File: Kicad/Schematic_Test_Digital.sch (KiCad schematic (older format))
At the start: 73 parts, among them J301 JST - 4x1, J302 JST - 4x1, J303 JST - 5x1, J304 JST - 5x1, SW301 RESET PUSH, U301 TSX-3225, U302 LIS3MDLTR, U303 LSM6DS33TR, U304 74HC595PW,112, U305 74HC595PW,112, U306 74HC595PW,112

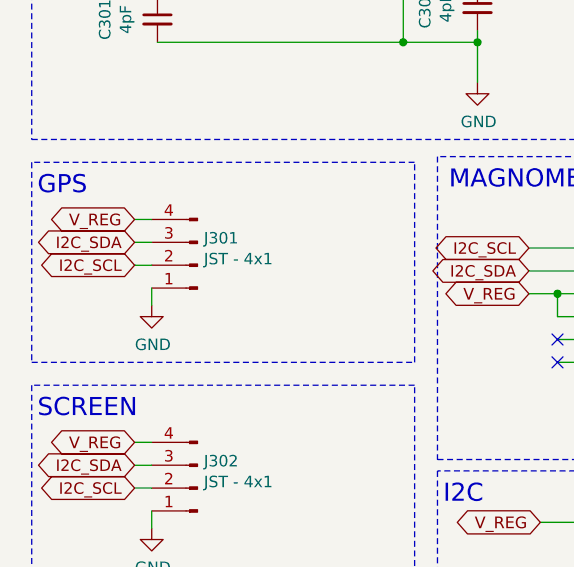
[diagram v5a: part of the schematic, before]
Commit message: PCB is likely complete.  Added USART for GPS.  Added background art and front label. Some leftover things are needed for the case.
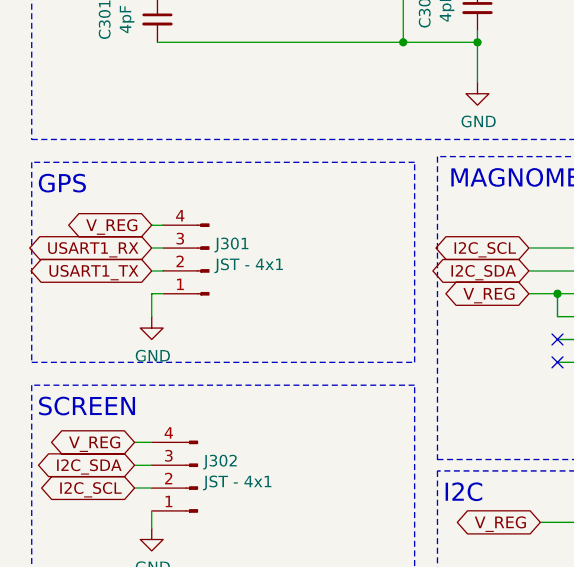
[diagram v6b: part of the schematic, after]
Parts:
- J301: part_details (none) -> USART; part_url (none) -> https://www.amazon.com/Microcontroller-Compatible-Sensitivi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
- J302: part_details (none) -> I2C; part_url https://www.amazon.com/WayinTop-Display-SSD1306-3-3V-5V-Ras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 -> https://www.amazon.com/Pieces-Display-Module-SSD1306-3-3V-5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
- J304: part_details (none) -> I2C; part_url (none) -> https://www.amazon.com/ARCELI-Joystick-Controller-Dual-axis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
- R302, R303: part_name Resistor - Pull up -> Resistor - Pull Up
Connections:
- net I2C_SCL: no longer J301.2 (Pin_2)
- net I2C_SDA: no longer J301.3 (Pin_3)
- new net USART1_RX: J301.3 (Pin_3)
- new net USART1_TX: J301.2 (Pin_2)
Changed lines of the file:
@@
 F 2 "Connector_JST:JST_EH_B5B-EH-A_1x05_P2.50mm_Vertical" H 1650 6025 50  0001 C CNN
 F 3 "~" H 1650 6025 50  0001 C CNN
-F 4 "" H 1650 6025 50  0001 C CNN "part_details"
-F 5 "" H 1650 6025 50  0001 C CNN "part_url"
+F 4 "I2C" H 1650 6025 50  0001 C CNN "part_details"
+F 5 "https://www.amazon.com/ARCELI-Joystick-Controller-Dual-axis-Breakout/dp/B077Z8QN3S" H 1650 6025 50  0001 C CNN "part_url"
 F 6 "Joystick Connector" H 1650 6025 50  0001 C CNN "part_name"
 	1    1650 6025
@@
 F 2 "Connector_JST:JST_EH_B4B-EH-A_1x04_P2.50mm_Vertical" H 1300 5050 50  0001 C CNN
 F 3 "~" H 1300 5050 50  0001 C CNN
-F 4 "" H 1300 5050 50  0001 C CNN "part_details"
-F 5 "https://www.amazon.com/WayinTop-Display-SSD1306-3-3V-5V-Raspberry/dp/B085NHJYBV/ref=pd_vtp_328_10?_encoding=UTF8&pd_rd_i=B085NHM5TC&pd_rd_r=7bdf7370-03dc-4b29-82c0-f607778b8952&pd_rd_w=HTH0F&pd_rd_wg=QAfMe&pf_rd_p=9f0d957d-c466-420a-817f-4adcb2657c85&pf_rd_r=2740EXSJPY7P7H0NYG2V&refRID=2740EXSJPY7P7H0NYG2V&th=1" H 1300 5050 50  0001 C CNN "part_url"
+F 4 "I2C" H 1300 5050 50  0001 C CNN "part_details"
+F 5 "https://www.amazon.com/Pieces-Display-Module-SSD1306-3-3V-5V/dp/B08CDN5PSJ/ref=pd_sbs_147_4/145-1111266-3690268?_encoding=UTF8&pd_rd_i=B08CDN5PSJ&pd_rd_r=0e37c7d0-00d4-4c6c-b496-f9da0ffda669&pd_rd_w=mtWFO&pd_rd_wg=RCtoO&pf_rd_p=703f3758-d945-4136-8df6-a43d19d750d1&pf_rd_r=FBPTKKC3JN25YH77MA03&psc=1&refRID=FBPTKKC3JN25YH77MA03" H 1300 5050 50  0001 C CNN "part_url"
 F 6 "Screen Connector" H 1300 5050 50  0001 C CNN "part_name"
 	1    1300 5050
@@
 Wire Notes Line
 	575  4500 2250 4500
-Wire Wire Line
-	1025 3875 1100 3875
-Wire Wire Line
-	1025 4075 1100 4075
-Wire Wire Line
-	1025 3975 1100 3975
 Wire Notes Line
 	2250 3625 575  3625
@@
 Wire Notes Line
 	575  3625 575  4500
-$Comp
-L power:GND #PWR?
-U 1 1 5F64B2EE
-P 1100 4250
-AR Path="/5F64B2EE" Ref="#PWR?"  Part="1"
-AR Path="/5F580392/5F64B2EE" Ref="#PWR0302"  Part="1"
-F 0 "#PWR0302" H 1100 4000 50  0001 C CNN
-F 1 "GND" H 1105 4077 50  0000 C CNN
-F 2 "" H 1100 4250 50  0001 C CNN
-F 3 "" H 1100 4250 50  0001 C CNN
-	1    1100 4250
-	1    0    0    -1
-$EndComp
-Wire Wire Line
-	1100 4175 1100 4250
-$Comp
-L Connector:Conn_01x04_Male J?
-U 1 1 5F64B2F5
-P 1300 4075
-AR Path="/5F64B2F5" Ref="J?"  Part="1"
-AR Path="/5F580392/5F64B2F5" Ref="J301"  Part="1"
-F 0 "J301" H 1272 3957 50  0000 R CNN
-F 1 "JST - 4x1" H 1272 4048 50  0000 R CNN
-F 2 "Connector_JST:JST_EH_B4B-EH-A_1x04_P2.50mm_Vertical" H 1300 4075 50  0001 C CNN
-F 3 "~" H 1300 4075 50  0001 C CNN
-F 4 "" H 1300 4075 50  0001 C CNN "part_details"
-F 5 "" H 1300 4075 50  0001 C CNN "part_url"
-F 6 "GPS Connector" H 1300 4075 50  0001 C CNN "part_name"
-	1    1300 4075
-	-1   0    0    1
-$EndComp
-Text Notes 600  3775 0    79   ~ 0
-GPS\n
-Text GLabel 1025 3975 0    50   BiDi ~ 0
-I2C_SDA
-Text GLabel 1025 4075 0    50   BiDi ~ 0
-I2C_SCL
-Text GLabel 1025 3875 0    51   BiDi ~ 0
-V_REG
 Connection ~ 10700 4900
 Wire Wire Line
@@
 F 2 "Resistor_SMD:R_1206_3216Metric_Pad1.42x1.75mm_HandSolder" V 3430 5525 50  0001 C CNN
 F 3 "~" H 3500 5525 50  0001 C CNN
-F 4 "Resistor - Pull up" H 3500 5525 50  0001 C CNN "part_name"
+F 4 "Resistor - Pull Up" H 3500 5525 50  0001 C CNN "part_name"
 F 5 "https://www.digikey.com/product-detail/en/yageo/RC1206JR-0710KL/311-10KERCT-ND/732156" H 3500 5525 50  0001 C CNN "part_url"
 	1    3500 5525
@@
 F 2 "Resistor_SMD:R_1206_3216Metric_Pad1.42x1.75mm_HandSolder" V 3080 5525 50  0001 C CNN
 F 3 "~" H 3150 5525 50  0001 C CNN
-F 4 "Resistor - Pull up" H 3150 5525 50  0001 C CNN "part_name"
+F 4 "Resistor - Pull Up" H 3150 5525 50  0001 C CNN "part_name"
 F 5 "https://www.digikey.com/product-detail/en/yageo/RC1206JR-0710KL/311-10KERCT-ND/732156" H 3150 5525 50  0001 C CNN "part_url"
 	1    3150 5525
@@
 Text GLabel 8300 3425 0    50   BiDi ~ 0
 RESET_N
+$Comp
+L power:GND #PWR?
+U 1 1 5F94CCE4
+P 1100 4300
+AR Path="/5F94CCE4" Ref="#PWR?"  Part="1"
+AR Path="/5F580392/5F94CCE4" Ref="#PWR0107"  Part="1"
+F 0 "#PWR0107" H 1100 4050 50  0001 C CNN
+F 1 "GND" H 1105 4127 50  0000 C CNN
+F 2 "" H 1100 4300 50  0001 C CNN
+F 3 "" H 1100 4300 50  0001 C CNN
+	1    1100 4300
+	1    0    0    -1
+$EndComp
+$Comp
+L Connector:Conn_01x04_Male J?
+U 1 1 5F94CCED
+P 1350 4100
+AR Path="/5F94CCED" Ref="J?"  Part="1"
+AR Path="/5F580392/5F94CCED" Ref="J301"  Part="1"
+F 0 "J301" H 1322 3982 50  0000 R CNN
+F 1 "JST - 4x1" H 1322 4073 50  0000 R CNN
+F 2 "Connector_JST:JST_EH_B4B-EH-A_1x04_P2.50mm_Vertical" H 1350 4100 50  0001 C CNN
+F 3 "~" H 1350 4100 50  0001 C CNN
+F 4 "USART" H 1350 4100 50  0001 C CNN "part_details"
+F 5 "https://www.amazon.com/Microcontroller-Compatible-Sensitivity-Navigation-Positioning/dp/B07P8YMVNT/ref=sr_1_3?dchild=1&keywords=arduino%2Bgps&qid=1601007680&sr=8-3&th=1" H 1350 4100 50  0001 C CNN "part_url"
+F 6 "GPS Connector" H 1350 4100 50  0001 C CNN "part_name"
+	1    1350 4100
+	-1   0    0    1
+$EndComp
+Text Notes 600  3775 0    79   ~ 0
+GPS\n
+Text GLabel 1100 3900 0    51   BiDi ~ 0
+V_REG
+Text GLabel 1100 4000 0    50   BiDi ~ 0
+USART1_RX
+Text GLabel 1100 4100 0    50   BiDi ~ 0
+USART1_TX
+Wire Wire Line
+	1100 3900 1150 3900
+Wire Wire Line
+	1100 4000 1150 4000
+Wire Wire Line
+	1100 4100 1150 4100
+Wire Wire Line
+	1150 4200 1100 4200
+Wire Wire Line
+	1100 4200 1100 4300
 $EndSCHEMATC

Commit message: Purchases made, case ordered, PCB ordered, parts ordered, money not happy.
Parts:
- removed C309: 100nF, Capacitor_SMD:C_0805_2012Metric_Pad1.15x1.40mm_HandSolder, symbol Device:C
- removed C310: 1uF, Capacitor_SMD:C_0805_2012Metric_Pad1.15x1.40mm_HandSolder, symbol Device:C
- removed U302: LIS3MDLTR, Package_LGA:LGA-12_2x2mm_P0.5mm, symbol StarGazer:LIS3MDL
- added U302: MMC5603NJ, Kicad:BGA_2_2, symbol StarGazer:MMC5603NJ
- C301, C303: PURCHASED (none) -> 6x IMPORT
- C302: PURCHASED (none) -> 12x
- C304: value 100nF -> 2.2uF; PURCHASED (none) -> 6x
- C305: PURCHASED (none) -> 6x
- C306, C307, C308, U304, U305, U306: PURCHASED (none) -> 9x
- D301, D302, D303, D304, D305, D306, D307, D308, D309, D310, D311, D312, D313, D314, D315, D316, D317, D318, D319, D320, D321, D322, D323, D324: PURCHASED (none) -> 72x
- J301: PURCHASED (none) -> 2x
- J302: PURCHASED (none) -> 5x
- J303: PURCHASED (none) -> 1x
- J304: PURCHASED (none) -> 10x
- R301, R302, R303: PURCHASED (none) -> 24x
- R304, R305, R306, R307, R308, R309, R310, R311, R312, R313, R314, R315, R316, R317, R318, R319, R320, R321, R322, R323, R324, R325, R326, R327: PURCHASED (none) -> 72 (up to 100)
- RV301, SW301, U301, U303: PURCHASED (none) -> 3x
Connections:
- net GND: now also U302.A1 (VSA)
- net I2C_SCL: now also U302.A2 (SCL)
- net I2C_SDA: now also U302.B2 (SDA)
- net V_REG: now also C304.2, U302.B1 (VDD)
- no-connect marks 5 -> 3
